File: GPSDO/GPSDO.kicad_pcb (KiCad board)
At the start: 2 copper layers, 86 parts, among them IC7 74HC14, J1 Conn_01x01_Pin, J2 SolderJumper_3_Open, J3 SolderJumper_2_Open, K1 Conn_01x04, K2 Conn_01x01_Pin, K3 Conn_01x02, K4 Conn_Coaxial, K5 Jumper_3_Open, K6 Conn_Coaxial, K7 Conn_01x02, K8 Conn_02x03_Odd_Even, K9 Conn_Coaxial, SW1 SW_Nidec_CAS-120A1, U1 LM7805_TO220, U2 DAC8571IDGK, U3 Pico, U4 AD8620, U5 74LVC2G86

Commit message: Changed VCC network, added ICS501 frequency multiplier
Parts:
- removed TP1, TP2, TP4, TP5: Conn_01x01_Pin, TestPoint:TestPoint_Pad_D1.0mm
- moved K9 274.0 mm to (73.1, 12.3), turned to -90 degrees
- moved K4 245.0 mm to (113.1, 12.3), turned to -90 degrees
- moved R26 241.1 mm to (68.5, 22.1), turned to -90 degrees
- moved C17 240.6 mm to (121.0, 73.0)
- moved C12 238.7 mm to (85.5, 18.0)
- moved C15 238.7 mm to (96.0, 32.4)
- moved C16 238.7 mm to (85.5, 29.5)
- moved IC2 238.7 mm to (92.3, 23.4)
- moved R14 238.7 mm to (91.5, 29.4)
- moved R17 238.7 mm to (100.5, 29.4)
- moved R8 238.7 mm to (74.0, 17.0)
- moved RV1 238.7 mm to (80.5, 30.5)
- moved RV2 238.7 mm to (80.5, 16.9)
- moved IC7 238.0 mm to (63.5, 31.0), turned to 180 degrees
- moved R24 236.3 mm to (65.0, 22.1), turned to -90 degrees
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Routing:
- net Net-(OCXO2-10MHz): track 0.00 -> 45.7 mm
- net Net-(OCXO2-VCC): track 0.00 -> 40.7 mm
- net Net-(IC6A-1B): track 0.00 -> 39.8 mm
- net Net-(K6-In): track 0.00 -> 37.8 mm, vias 0 -> 1
- net Net-(OCXO2-Vcont): track 5.53 -> 32.0 mm, vias 0 -> 1
- net Net-(IC1-COMP_in): track 20.9 -> 46.2 mm
- net Net-(K4-In): track 0.00 -> 24.4 mm, vias 0 -> 2
- net Net-(R8-Pad2): track 4.97 -> 29.3 mm, vias 0 -> 1
- net Net-(K8-Pin_5): track 0.00 -> 22.5 mm, vias 0 -> 1
- net Net-(IC2-Pad6): track 0.00 -> 10.2 mm
- net Net-(IC1-INH): track 37.1 -> 29.4 mm
- net Net-(IC2-Pad7): track 0.00 -> 5.03 mm
- net Net-(IC1-SIG_in): track 21.8 -> 17.0 mm
- net Net-(C3-Pad1): track 3.90 -> 0.00 mm
- net Net-(IC7-Pad12): track 0.00 -> 3.71 mm
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
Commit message: added voltage reference to DAC
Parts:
- removed C24, C25, C26: 100n, Capacitor_SMD:C_1210_3225Metric_Pad1.33x2.70mm_HandSolder
- removed J1: Conn_01x01_Pin, TestPoint:TestPoint_Pad_D1.0mm
- removed K8: Conn_02x03_Odd_Even, Connector_IDC:IDC-Header_2x03_P2.54mm_Vertical
- removed L4, L6: 10µ, Inductor_SMD:L_Cenker_CKCS6045
- removed SW1: SW_Nidec_CAS-120A1, Button_Switch_THT:SW_E-Switch_EG1271_SPDT
- added C23: 100n, Capacitor_SMD:C_1210_3225Metric_Pad1.33x2.70mm_HandSolder, F.Cu at (-39.8, 2.50)
- added C35: 100n, Capacitor_SMD:C_1210_3225Metric_Pad1.33x2.70mm_HandSolder, F.Cu at (-57.6, 64.9)
- added C36: 100n, Capacitor_SMD:C_1210_3225Metric_Pad1.33x2.70mm_HandSolder, F.Cu at (82.1, 135.7)
- added C37: 100n, Capacitor_SMD:C_1210_3225Metric_Pad1.33x2.70mm_HandSolder, F.Cu at (82.1, 143.6)
- added C38: 100n, Capacitor_SMD:C_1210_3225Metric_Pad1.33x2.70mm_HandSolder, F.Cu at (121.2, 102.7)
- added C39: 100n, Capacitor_SMD:C_1210_3225Metric_Pad1.33x2.70mm_HandSolder, F.Cu at (-83.4, 81.6)
- added J11: JP1, Connector_PinHeader_2.54mm:PinHeader_2x03_P2.54mm_Vertical, F.Cu at (-41.6, 45.6)
- added JP1: Jumper_2_Open, Connector_PinHeader_2.54mm:PinHeader_1x02_P2.54mm_Vertical, F.Cu at (37.1, 35.8)
- added K10: Conn_Coaxial, Connector_Coaxial:SMA_Molex_73251-1153_EdgeMount_Horizontal, F.Cu at (-83.6, 60.1)
- added L10: 10µ, Inductor_SMD:L_0805_2012Metric_Pad1.15x1.40mm_HandSolder, F.Cu at (-40.8, 90.4)
- added L7: 10µ, Inductor_SMD:L_0805_2012Metric_Pad1.15x1.40mm_HandSolder, F.Cu at (82.2, 139.7)
- added L8: 10µ, Inductor_SMD:L_0805_2012Metric_Pad1.15x1.40mm_HandSolder, F.Cu at (-40.8, 84.5)
- added L9: 10µ, Inductor_SMD:L_0805_2012Metric_Pad1.15x1.40mm_HandSolder, F.Cu at (124.4, 102.7)
- added R18: 50, Resistor_SMD:R_1210_3225Metric_Pad1.30x2.65mm_HandSolder, F.Cu at (-65.5, 28.5)
- added R19: 50, Resistor_SMD:R_1210_3225Metric_Pad1.30x2.65mm_HandSolder, F.Cu at (-65.5, 32.7)
- added R3: 100k, Resistor_SMD:R_1210_3225Metric_Pad1.30x2.65mm_HandSolder, F.Cu at (-34.6, 4.10)
- added R35: 10k, Resistor_SMD:R_1210_3225Metric_Pad1.30x2.65mm_HandSolder, F.Cu at (27.4, 58.8)
- added R36: 10k, Resistor_SMD:R_1210_3225Metric_Pad1.30x2.65mm_HandSolder, F.Cu at (23.8, 58.8)
- added R37: 10k, Resistor_SMD:R_1210_3225Metric_Pad1.30x2.65mm_HandSolder, F.Cu at (33.2, 58.8)
- added R38: 4.7k, Resistor_SMD:R_1210_3225Metric_Pad1.30x2.65mm_HandSolder, F.Cu at (-53.6, 24.3)
- added R39: 4.7k, Resistor_SMD:R_1210_3225Metric_Pad1.30x2.65mm_HandSolder, F.Cu at (-53.6, 28.5)
- added R40: 50, Resistor_SMD:R_1210_3225Metric_Pad1.30x2.65mm_HandSolder, F.Cu at (-53.6, 32.7)
- added R7: 100k, Resistor_SMD:R_1210_3225Metric_Pad1.30x2.65mm_HandSolder, F.Cu at (-77.4, 41.1)
- added U8: U1, Package_SO:SOIC-8_3.9x4.9mm_P1.27mm, F.Cu at (-40.1, 9.70)
- added U9: CAT24C128, Package_SO:SOIC-8_3.9x4.9mm_P1.27mm, F.Cu at (28.8, 50.0)
- C15: value 0.1u -> 100n
- L1, L5: footprint Inductor_SMD:L_Neosid_SM-PIC0612H -> Inductor_SMD:L_0805_2012Metric_Pad1.15x1.40mm_HandSolder
- L2: footprint Inductor_SMD:L_Cenker_CKCS6045 -> Inductor_SMD:L_0805_2012Metric_Pad1.15x1.40mm_HandSolder
- moved K4 196.8 mm to (-83.6, 20.4), turned to 0 degrees
- moved C12 193.2 mm to (-95.4, 85.8), turned to 0 degrees
- moved C15 188.9 mm to (-89.4, 68.8)
- moved C16 180.2 mm to (-89.4, 73.1), turned to 0 degrees
- moved K6 178.0 mm to (-83.6, 33.6), turned to 0 degrees
- moved U5 176.7 mm to (-59.8, 97.5)
- moved RV2 171.4 mm to (-73.7, 91.9), turned to 0 degrees
- moved R17 166.0 mm to (-65.5, 24.3), turned to 0 degrees
- moved RV1 163.8 mm to (-73.7, 85.8), turned to 0 degrees
- moved R14 163.3 mm to (-71.4, 41.1), turned to 0 degrees
- moved K9 160.4 mm to (-83.6, 46.9), turned to 0 degrees
- moved IC2 150.4 mm to (-40.2, 94.3)
- moved C20 149.8 mm to (102.5, 227.6), turned to 90 degrees
- moved R8 145.4 mm to (-71.4, 15.9)
- moved K7 131.7 mm to (77.6, 239.2)
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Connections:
- C15 pad 1: /VCC -> Net-(IC2A-V+)
- C21 pad 1: /VCC_1 -> /VCC
- C22 pad 1: /VCC_1 -> Net-(OCXO2-Vcont)
- C7 pad 1: Net-(IC1-LD) -> /VCC
- C8 pad 1: Net-(IC1-LD) -> /VCC
- IC2 pad 8: /VCC -> Net-(IC2A-V+)
- IC3 pad 16: /VCC_1 -> Net-(IC3C-VCC)
- IC6 pad 16: /VCC_1 -> Net-(IC3C-VCC)
- IC7 pad 14: /VCC_1 -> Net-(IC7G-VCC)
- L2 pad 1: /VCC -> Net-(U8-OE)
- L2 pad 2: Net-(IC1-LD) -> /VCC
- R14 pad 1: /VCC -> Net-(IC2A-V+)
- R22 pad 1: /VCC_1 -> /VCC
- R28 pad 1: Net-(K8-Pin_5) -> Net-(K9-In)
- RV1 pad 3: Net-(K6-In) -> Net-(R19-Pad1)
- U1 pad 3: Net-(SW1-A) -> /VCC
- U3 pad 26: unconnected-(U3-GPIO20-Pad26) -> Net-(U3-GPIO20)
- U3 pad 27: unconnected-(U3-GPIO21-Pad27) -> Net-(U3-GPIO21)
- U3 pad 40: Net-(IC1-LD) -> /VCC
- U3 pad 5: unconnected-(U3-GPIO3-Pad5) -> Net-(IC1-LD)
- U5 pad 3: Net-(K4-In) -> Net-(R18-Pad1)
- U5 pad 6: Net-(K6-In) -> Net-(R19-Pad1)
- U5 pad 7: Net-(K6-In) -> Net-(R19-Pad1)
- U5 pad 8: /VCC_1 -> Net-(U5C-VCC)
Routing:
- net Net-(IC1-COMP_in): track 46.2 -> 0.00 mm
- net Net-(K6-In): track 37.8 -> 0.00 mm, vias 1 -> 0
- net Net-(OCXO2-10MHz): track 45.7 -> 12.6 mm
- net Net-(R8-Pad2): track 29.3 -> 0.00 mm, vias 1 -> 0
- net Net-(JP1-B): track 0.00 -> 28.5 mm
- net Net-(K1-Pin_1): track 49.8 -> 78.2 mm
- net Net-(K4-In): track 24.4 -> 0.00 mm, vias 2 -> 0
- net Net-(K8-Pin_5): track 22.5 -> 0.00 mm, vias 1 -> 0
- net Net-(IC1-LD): track 21.2 -> 0.00 mm
- net Net-(IC6A-1B): track 39.8 -> 18.9 mm
- net Net-(OCXO2-VCC): track 40.7 -> 19.9 mm
- net Net-(IC3C-VCC): track 0.00 -> 18.8 mm
- net /VCC_1: track 18.1 -> 0.00 mm
- net Net-(J2-C): track 23.8 -> 6.46 mm
- net /VCC/2: track 16.9 -> 0.00 mm
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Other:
- board text added: "10MHz_out"
- board text added: "COUNTER"
- board text added: "I2C"
- board text added: "LPF"
- board text added: "OCXO"
- board text added: "OCXO CONTROL"
- board text added: "OCXO_out"
- board text added: "PHASE COMP"
- board text added: "PPS"
- board text added: "SCHMITT TRIG"
- board text added: "VCC"
- board text added: "V_ctrl"
- board text added: "comp"
- board text added: "counter_in"
- board text added: "f_comp"

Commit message: Layout almost done (GND plane & edge cuts missing), replaced counters with PIC 12F675 MCU for more flexible down conversion and less ICs on the PCB
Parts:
- removed C36, C37: 100n, Capacitor_SMD:C_1210_3225Metric_Pad1.33x2.70mm_HandSolder
- removed IC3, IC6: ~, Package_SO:SOIC-16_3.9x9.9mm_P1.27mm
- removed J11: JP1, Connector_PinHeader_2.54mm:PinHeader_2x03_P2.54mm_Vertical
- removed J2: SolderJumper_3_Open, Jumper:SolderJumper-3_P1.3mm_Open_RoundedPad1.0x1.5mm_NumberLabels
- removed J3: SolderJumper_2_Open, Jumper:SolderJumper-2_P1.3mm_Open_RoundedPad1.0x1.5mm
- removed K2: Conn_01x01_Pin, TestPoint:TestPoint_Loop_D2.50mm_Drill1.85mm
- added C24: 100n, Capacitor_SMD:C_1210_3225Metric_Pad1.33x2.70mm_HandSolder, F.Cu at (149.2, 100.4)
- added C25: 100n, Capacitor_SMD:C_1210_3225Metric_Pad1.33x2.70mm_HandSolder, F.Cu at (138.6, 100.4)
- added C26: 100n, Capacitor_SMD:C_1210_3225Metric_Pad1.33x2.70mm_HandSolder, F.Cu at (85.3, 107.2)
- added JP2: Conn_02x03_Odd_Even, Connector_PinHeader_2.54mm:PinHeader_2x03_P2.54mm_Vertical, F.Cu at (116.1, 116.6)
- added K8: Conn_Coaxial, Connector_Coaxial:SMA_Molex_73251-1153_EdgeMount_Horizontal, F.Cu at (100.5, 50.1)
- added L4: 10µ, Inductor_SMD:L_0805_2012Metric_Pad1.15x1.40mm_HandSolder, F.Cu at (145.6, 100.4)
- added L6: 10µ, Inductor_SMD:L_0805_2012Metric_Pad1.15x1.40mm_HandSolder, F.Cu at (135.0, 100.3)
- added R20: 1k, Resistor_SMD:R_0805_2012Metric_Pad1.20x1.40mm_HandSolder, F.Cu at (154.3, 66.9)
- added R21: 240, Resistor_SMD:R_0805_2012Metric_Pad1.20x1.40mm_HandSolder, F.Cu at (145.2, 116.7)
- added R30: 240, Resistor_SMD:R_0805_2012Metric_Pad1.20x1.40mm_HandSolder, F.Cu at (142.5, 116.7)
- added R31: 240, Resistor_SMD:R_0805_2012Metric_Pad1.20x1.40mm_HandSolder, F.Cu at (139.8, 116.7)
- added R32: 240, Resistor_SMD:R_0805_2012Metric_Pad1.20x1.40mm_HandSolder, F.Cu at (137.1, 116.7)
- added R33: 240, Resistor_SMD:R_0805_2012Metric_Pad1.20x1.40mm_HandSolder, F.Cu at (152.8, 116.7)
- added R34: 240, Resistor_SMD:R_0805_2012Metric_Pad1.20x1.40mm_HandSolder, F.Cu at (150.1, 116.7)
- added R41: 240, Resistor_SMD:R_0805_2012Metric_Pad1.20x1.40mm_HandSolder, F.Cu at (155.5, 116.7)
- added R42: 240, Resistor_SMD:R_0805_2012Metric_Pad1.20x1.40mm_HandSolder, F.Cu at (124.1, 116.7)
- added R43: 240, Resistor_SMD:R_0805_2012Metric_Pad1.20x1.40mm_HandSolder, F.Cu at (129.5, 116.7)
- added U10: 74HC14, Package_SO:SOIC-14_3.9x8.7mm_P1.27mm, F.Cu at (135.9, 108.7)
- added U11: PIC12F675-xP, Package_DIP:DIP-8_W7.62mm, F.Cu at (90.1, 108.5)
- added U6: LM4040DBZ-4.1, Package_TO_SOT_SMD:SOT-23, F.Cu at (154.1, 72.2)
- added U7: 74HC14, Package_SO:SOIC-14_3.9x8.7mm_P1.27mm, F.Cu at (146.4, 108.7)
- C11, C3: footprint Capacitor_THT:C_Rect_L7.2mm_W3.5mm_P5.00mm_FKS2_FKP2_MKS2_MKP2 -> Capacitor_THT:C_Rect_L7.2mm_W5.5mm_P5.00mm_FKS2_FKP2_MKS2_MKP2
- C17, C2, C21, C7: footprint Capacitor_THT:CP_Radial_D6.3mm_P2.50mm -> Capacitor_SMD:CP_Elec_4x5.3
- C18, C5: footprint Capacitor_THT:CP_Radial_D10.0mm_P5.00mm -> Capacitor_SMD:CP_Elec_6.3x9.9
- D1: footprint Diode_SMD:D_SMA-SMB_Universal_Handsoldering -> Diode_SMD:D_SOD-123F
- D2: footprint Diode_THT:D_DO-15_P10.16mm_Horizontal -> Diode_SMD:D_SMB
- K7: footprint Connector_BarrelJack:BarrelJack_CUI_PJ-102AH_Horizontal -> Connector_AMASS:AMASS_XT30PW-M_1x02_P2.50mm_Horizontal
- R1, R10, R11, R12, R13, R14, R15, R16, R17, R2, R22, R23, R24, R25, R26, R27, R28, R29, R3, R35, R36, R37, R38, R39, R4, R5, R6, R7, R8, R9: footprint Resistor_SMD:R_1210_3225Metric_Pad1.30x2.65mm_HandSolder -> Resistor_SMD:R_0805_2012Metric_Pad1.20x1.40mm_HandSolder
- R18, R19, R40: value 50 -> 240; footprint Resistor_SMD:R_1210_3225Metric_Pad1.30x2.65mm_HandSolder -> Resistor_SMD:R_0805_2012Metric_Pad1.20x1.40mm_HandSolder
- RV1: footprint Potentiometer_THT:Potentiometer_Bourns_3266Y_Vertical -> Potentiometer_SMD:Potentiometer_Bourns_3314S_Horizontal
- RV2: footprint Potentiometer_THT:Potentiometer_Bourns_3266Y_Vertical -> Potentiometer_SMD:Potentiometer_Bourns_3314J_Vertical
- moved K6 253.9 mm to (154.1, 122.9), turned to 90 degrees
- moved K4 247.0 mm to (141.1, 122.9), turned to 90 degrees
- moved C15 244.6 mm to (154.5, 87.4)
- moved R19 238.9 mm to (158.2, 116.7), turned to 90 degrees
- moved C12 238.8 mm to (143.3, 80.4), turned to -90 degrees
- moved C39 238.1 mm to (154.5, 92.2), turned to 180 degrees
- moved C16 233.1 mm to (143.2, 88.3), turned to -90 degrees
- moved R14 223.6 mm to (147.8, 85.3), turned to 180 degrees
- moved R17 221.2 mm to (147.8, 82.8), turned to 180 degrees
- moved K10 220.8 mm to (128.1, 122.9), turned to 90 degrees
- moved R18 216.5 mm to (132.2, 116.7), turned to 90 degrees
- moved RV2 212.3 mm to (138.3, 80.4), turned to 180 degrees
- moved RV1 211.9 mm to (138.2, 88.3), turned to 180 degrees
- moved R7 210.0 mm to (120.4, 111.7), turned to 180 degrees
- moved U5 207.6 mm to (147.7, 93.7)
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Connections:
- C13 pad 1: Net-(U2-V_{DD}) -> Net-(U4C-V+)
- C14 pad 1: Net-(U2-V_{DD}) -> Net-(U4C-V+)
- L5 pad 1: Net-(U2-V_{DD}) -> Net-(U4C-V+)
- R18 pad 1: Net-(R18-Pad1) -> Net-(K10-In)
- R18 pad 2: Net-(K4-In) -> Net-(R18-Pad2)
- R19 pad 1: Net-(R19-Pad1) -> Net-(K6-In)
- R19 pad 2: Net-(K6-In) -> Net-(R19-Pad2)
- R3 pad 1: /VCC -> Net-(U8-OE)
- R40 pad 1: Net-(U8-CLK) -> Net-(K10-In)
- R40 pad 2: Net-(K10-In) -> Net-(R40-Pad2)
- RV1 pad 3: Net-(R19-Pad1) -> Net-(K6-In)
- U4 pad 8: Net-(U2-V_{DD}) -> Net-(U4C-V+)
- U5 pad 3: Net-(R18-Pad1) -> Net-(U10-Pad1)
- U5 pad 6: Net-(R19-Pad1) -> Net-(K6-In)
- U5 pad 7: Net-(R19-Pad1) -> Net-(U5-Pad7)
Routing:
- net /VCC: track 55.3 -> 254.8 mm, vias 0 -> 18
- net /comp: track 0.00 -> 73.5 mm, vias 0 -> 2
- net Net-(K6-In): track 0.00 -> 71.6 mm
- net Net-(IC1-LD): track 0.00 -> 62.9 mm, vias 0 -> 1
- net Net-(U2-SDA): track 4.46 -> 67.2 mm, vias 0 -> 2
- net Net-(K9-In): track 14.0 -> 71.8 mm, vias 0 -> 5
- net Net-(U2-SCL): track 8.39 -> 66.0 mm, vias 0 -> 4
- net Net-(R8-Pad2): track 0.00 -> 50.8 mm, vias 0 -> 3
- net Net-(U11-GP0): track 6.46 -> 57.2 mm, vias 0 -> 1
- net Net-(IC3A-1B): track 31.3 -> 0.00 mm, vias 2 -> 0
- net Net-(U10-Pad1): track 0.00 -> 31.1 mm, vias 0 -> 2
- net Net-(JP2-Pin_3): track 0.00 -> 30.0 mm, vias 0 -> 1
- net Net-(U5-Pad7): track 0.00 -> 29.3 mm, vias 0 -> 2
- net Net-(OCXO2-10MHz): track 12.6 -> 40.8 mm
- net Net-(K10-In): track 0.00 -> 26.5 mm
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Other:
- board text added: "Haben die grauen Flächen Einfluss auf Cu-Layer?"
- board text removed: "10MHz_out"
- board text removed: "COUNTER"
- board text removed: "I2C"
- board text removed: "LPF"
- board text removed: "OCXO"
- board text removed: "OCXO CONTROL"
- board text removed: "OCXO_out"
- board text removed: "PHASE COMP"
- board text removed: "PPS"
- board text removed: "SCHMITT TRIG"
- board text removed: "VCC"
- board text removed: "V_ctrl"
- board text removed: "comp"
- board text removed: "counter_in"
- board text removed: "f_comp"

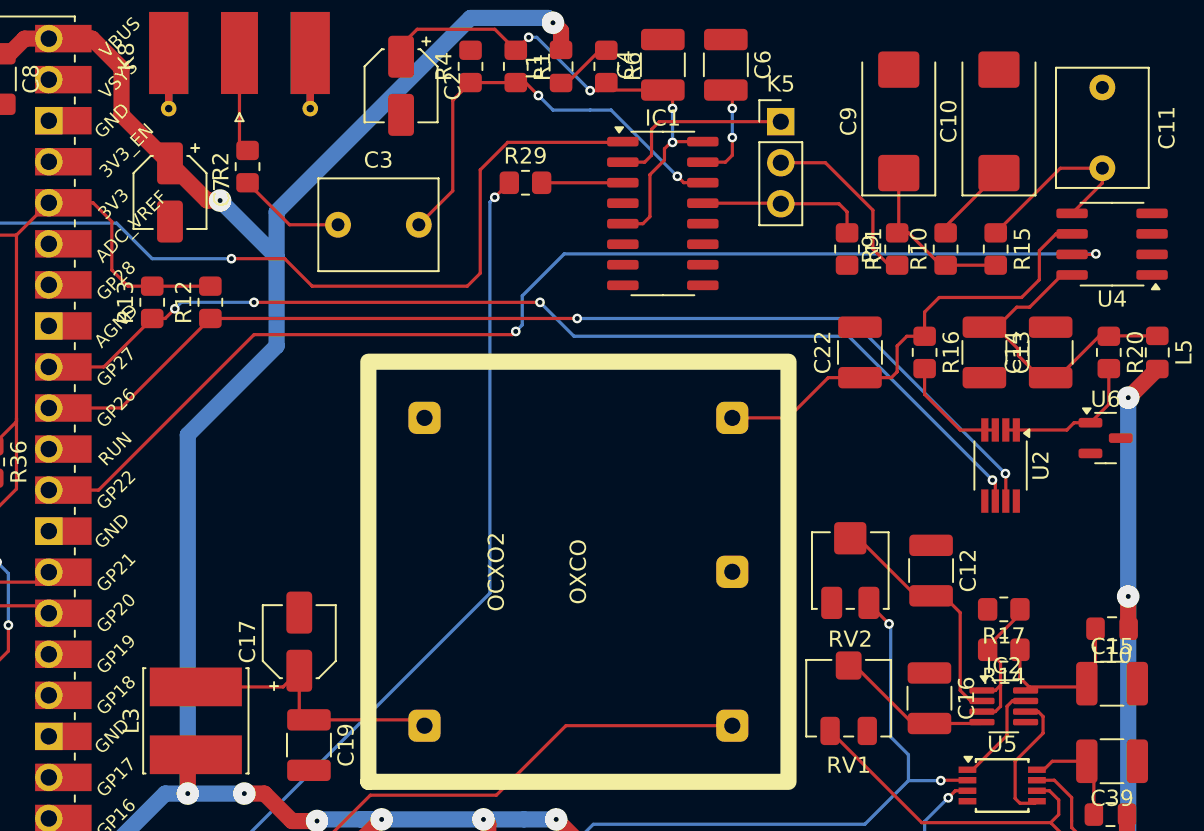
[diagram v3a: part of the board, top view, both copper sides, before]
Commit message: VCC net width fix, added voltage dividers for Pico inputs
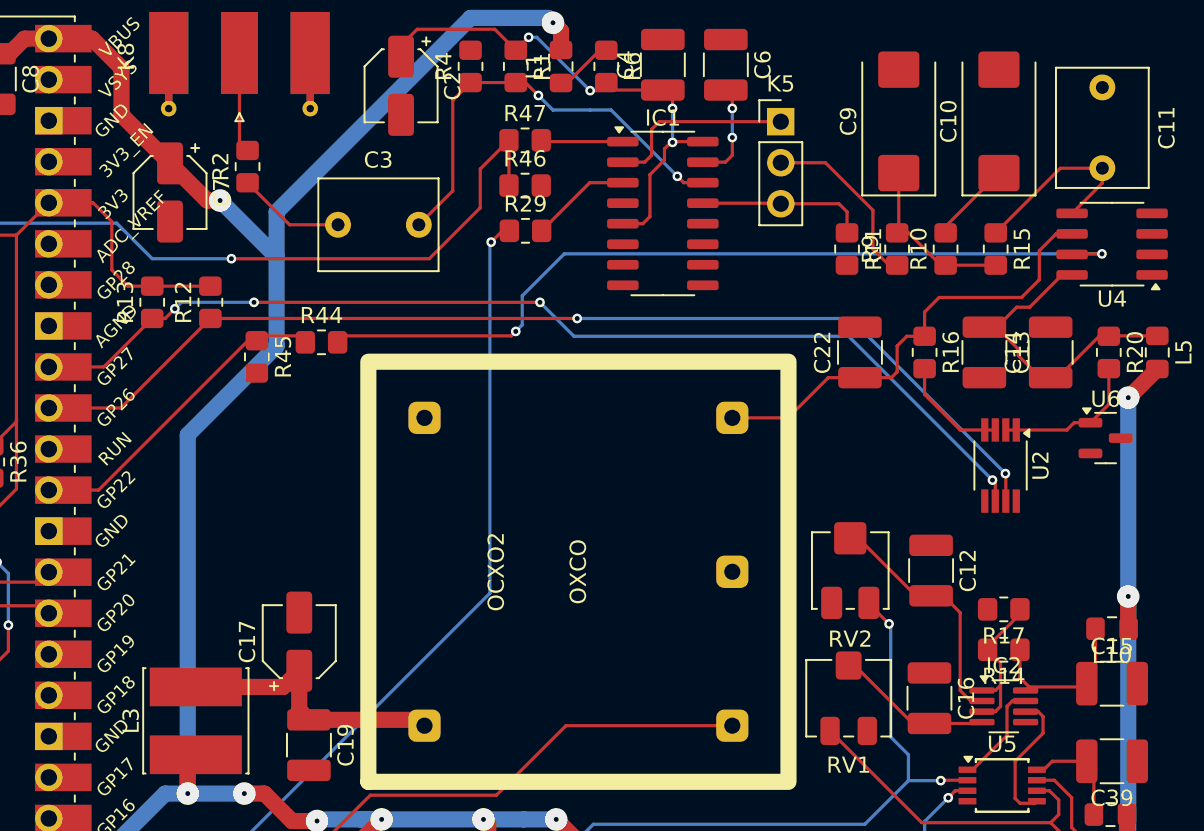
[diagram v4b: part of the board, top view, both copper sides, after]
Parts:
- added R44: 27k, Resistor_SMD:R_0805_2012Metric_Pad1.20x1.40mm_HandSolder, F.Cu at (105.6, 66.3)
- added R45: 47k, Resistor_SMD:R_0805_2012Metric_Pad1.20x1.40mm_HandSolder, F.Cu at (101.6, 67.2)
- added R46: 47k, Resistor_SMD:R_0805_2012Metric_Pad1.20x1.40mm_HandSolder, F.Cu at (118.2, 56.6)
- added R47: 27k, Resistor_SMD:R_0805_2012Metric_Pad1.20x1.40mm_HandSolder, F.Cu at (118.2, 53.8)
- moved R29 2.98 mm to (118.2, 59.4)
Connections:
- U3 pad 29: /comp -> Net-(U3-GPIO22)
- U3 pad 5: Net-(IC1-LD) -> Net-(U3-GPIO3)
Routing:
- net Net-(IC1-LD): track 62.9 -> 5.15 mm, vias 1 -> 0
- net Net-(U3-GPIO3): track 0.00 -> 54.9 mm, vias 0 -> 1
- net /comp: track 73.5 -> 52.5 mm
- net Net-(U3-GPIO22): track 0.00 -> 20.0 mm
- net Net-(U11-GP0): track 57.2 -> 54.4 mm
- net Net-(IC1-COMP_in): track 5.03 -> 6.27 mm
